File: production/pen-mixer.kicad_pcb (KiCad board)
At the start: 4 copper layers, 11 x 42 mm, 28 parts, among them J1 USB-C 16P, J2 BAT, U1 ISP1807-LR, U2 LSM6DS3TR-C, U3 MCP73831T-2ACI/OT, U4 TPS7A0533PDBV

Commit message: board fully routed verified
Claude-Session: https://claude.ai/code/session_01RCYT2QSY7BVZDeTyE9KrC4
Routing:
- net VBAT: track 39.4 -> 42.4 mm
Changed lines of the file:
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@@
+	)
+	(segment
+		(start 103.8 67.3)
+		(end 103.5 67.61)
+		(width 0.15)
+		(layer "F.Cu")
+		(net "VBAT")
 	)
 	(segment
@@
 	)
 	(segment
+		(start 103.5 64.89)
+		(end 103.8 65.2)
+		(width 0.15)
+		(layer "F.Cu")
+		(net "VBAT")
+	)
+	(segment
 		(start 103.501 64.8928)
 		(end 101.974 63.3652)
 		(width 0.15)
 		(layer "F.Cu")
+		(net "VBAT")
+	)
+	(segment
+		(start 103.8 65.2)
+		(end 103.8 67.3)
+		(width 0.15)
+		(layer "F.Cu")

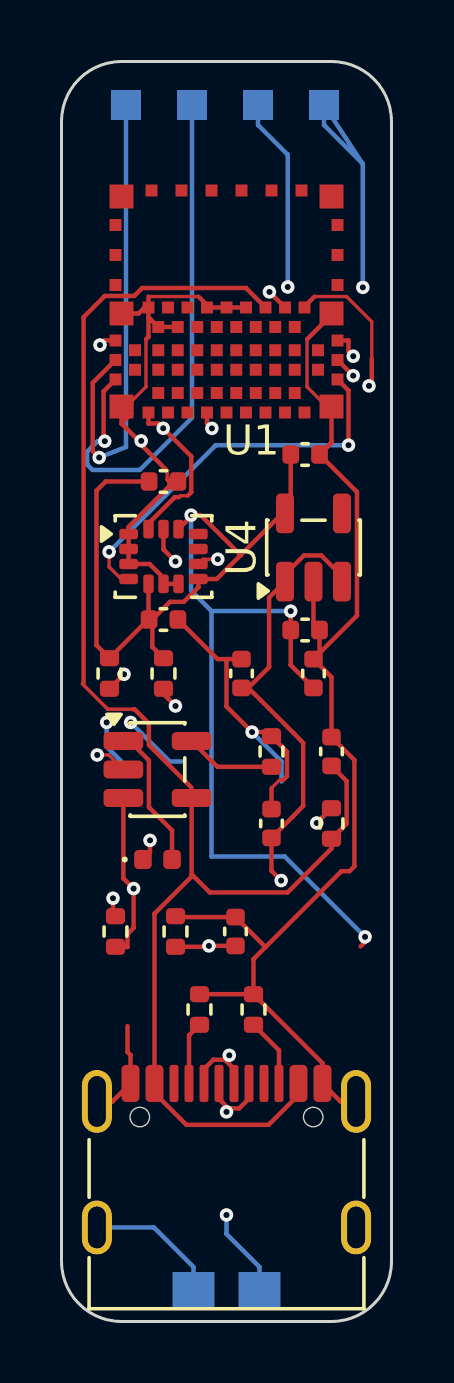
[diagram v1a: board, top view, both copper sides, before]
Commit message: unroute board
Claude-Session: https://claude.ai/code/session_01RCYT2QSY7BVZDeTyE9KrC4
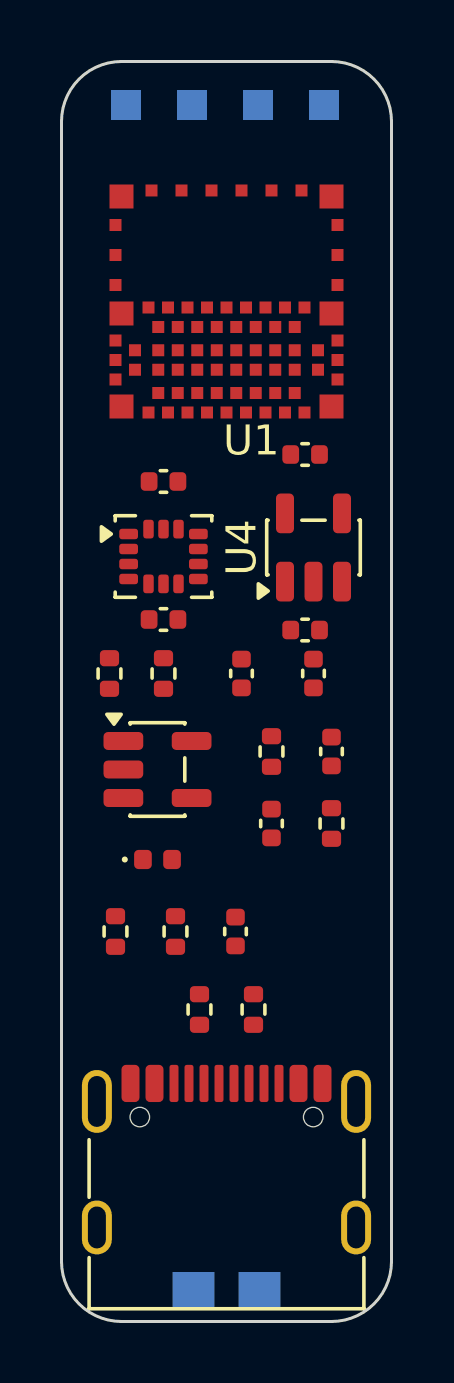
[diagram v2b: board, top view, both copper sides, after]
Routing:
- net GND: track 142.5 -> 0.00 mm, vias 4 -> 0
- net +3V3: track 77.3 -> 0.00 mm, vias 5 -> 0
- net VBUS: track 49.5 -> 0.00 mm
- net VBAT: track 42.4 -> 0.00 mm, vias 3 -> 0
- net USB_DP: track 33.5 -> 0.00 mm, vias 2 -> 0
- net SWDCLK: track 30.5 -> 0.00 mm, vias 2 -> 0
- net USB_DM: track 29.2 -> 0.00 mm, vias 2 -> 0
- net SWDIO: track 26.8 -> 0.00 mm, vias 2 -> 0
- net VBAT_SENSE: track 24.1 -> 0.00 mm, vias 3 -> 0
- net SCL: track 17.1 -> 0.00 mm, vias 3 -> 0
- net SDA: track 14.9 -> 0.00 mm, vias 2 -> 0
- net IMU_INT1: track 13.1 -> 0.00 mm, vias 2 -> 0
- net IMU_INT2: track 9.44 -> 0.00 mm, vias 2 -> 0
- net LED_A: track 7.23 -> 0.00 mm, vias 2 -> 0
- net CHG_STAT: track 4.74 -> 0.00 mm
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
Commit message: clean full reroute zero violations
Claude-Session: https://claude.ai/code/session_01RCYT2QSY7BVZDeTyE9KrC4
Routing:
- net GND: track 0.00 -> 98.3 mm, vias 0 -> 1
- net +3V3: track 0.00 -> 52.7 mm, vias 0 -> 2
- net VBUS: track 0.00 -> 45.5 mm, vias 0 -> 3
- net VBAT: track 0.00 -> 41.4 mm, vias 0 -> 6
- net USB_DP: track 0.00 -> 31.7 mm, vias 0 -> 2
- net USB_DM: track 0.00 -> 29.8 mm, vias 0 -> 2
- net VBAT_SENSE: track 0.00 -> 22.3 mm, vias 0 -> 2
- net SCL: track 0.00 -> 19.3 mm, vias 0 -> 3
- net SDA: track 0.00 -> 14.9 mm, vias 0 -> 2
- net IMU_INT1: track 0.00 -> 12.7 mm, vias 0 -> 2
- net SWDCLK: track 0.00 -> 11.8 mm, vias 0 -> 1
- net SWDIO: track 0.00 -> 10.5 mm, vias 0 -> 2
- net LED_A: track 0.00 -> 10.1 mm, vias 0 -> 2
- net IMU_INT2: track 0.00 -> 10.0 mm, vias 0 -> 2
- net CHG_STAT: track 0.00 -> 5.07 mm
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
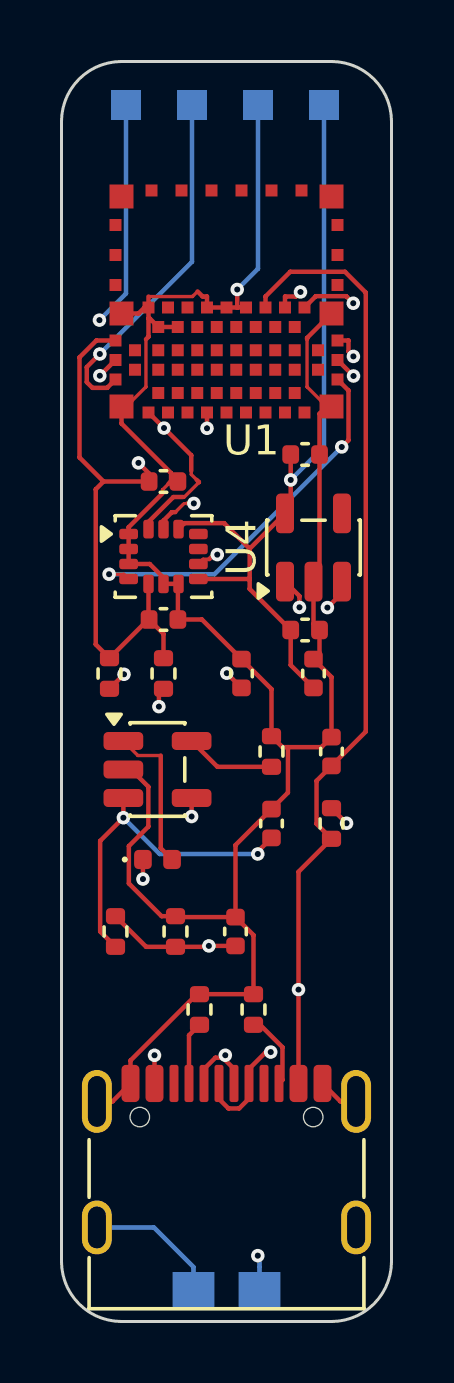
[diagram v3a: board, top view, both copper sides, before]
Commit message: fix wire tee gaps
Claude-Session: https://claude.ai/code/session_01RCYT2QSY7BVZDeTyE9KrC4
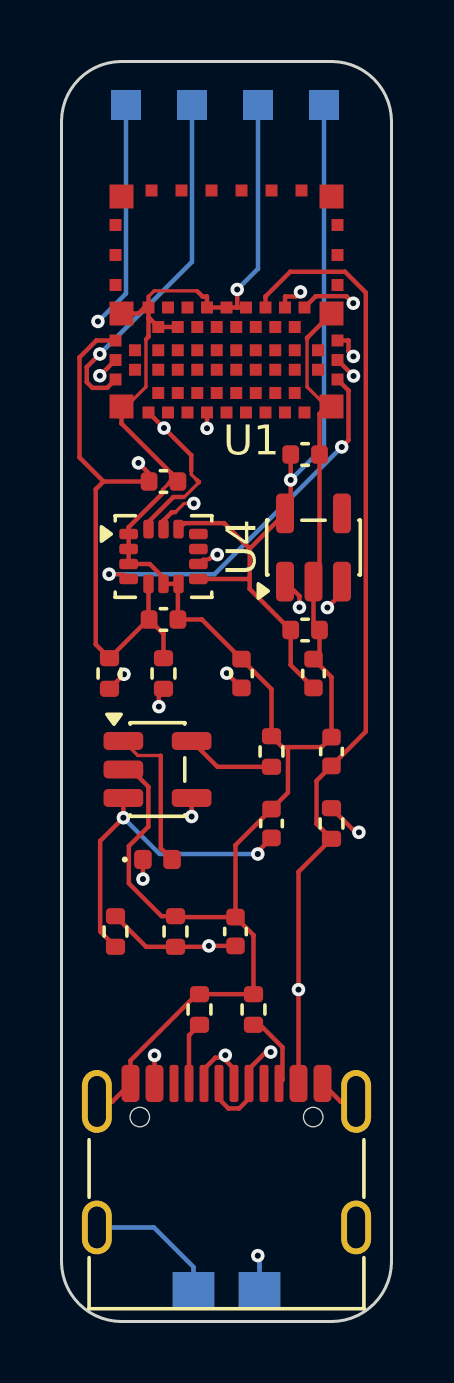
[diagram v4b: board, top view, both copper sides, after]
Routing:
- net LED_A: track 10.1 -> 11.1 mm
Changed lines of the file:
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@@
-	)
-	(segment
-		(start 100.1104 50.32)
-		(end 100.2804 50.15)
-		(width 0.1124)
-		(layer "F.Cu")
-		(net "GND")
 	)
 	(segment
@@
 	)
 	(segment
+		(start 100.2604 50.13)
+		(end 100.2804 50.15)
+		(width 0.1124)
+		(layer "F.Cu")
+		(net "GND")
+	)
+	(segment
 		(start 101.5452 71.0052)
 		(end 99.5752 71.0052)
@@
 		(end 101.8952 50.6852)
 		(width 0.15)
+		(layer "F.Cu")
+		(net "GND")
+	)
+	(segment
+		(start 98.6452 50.32)
+		(end 98.8352 50.13)
+		(width 0.1124)
 		(layer "F.Cu")
 		(net "GND")
@@
 	)
 	(segment
-		(start 98.6452 50.32)
-		(end 100.1104 50.32)
-		(width 0.1124)
-		(layer "F.Cu")
-		(net "GND")
-	)
-	(segment
 		(start 104.5852 53.9852)
 		(end 104.42 53.82)
 		(width 0.15)
+		(layer "F.Cu")
+		(net "GND")
+	)
+	(segment
+		(start 98.8352 50.13)
+		(end 100.2604 50.13)
+		(width 0.1124)
 		(layer "F.Cu")
 		(net "GND")
@@
 	)
 	(segment
-		(start 105.2465 67.8765)
+		(start 105.66 68.18)
+		(end 105.55 68.18)
+		(width 0.15)
+		(layer "F.Cu")
+		(net "LED_A")
+	)
+	(segment
+		(start 105.55 68.18)
 		(end 104.7452 67.3752)
 		(width 0.15)
@@
 	)
 	(via
-		(at 105.2465 67.8765)
+		(at 105.66 68.18)
 		(size 0.45)
 		(drill 0.2)
@@
 		(drill 0.2)
 		(layers "F.Cu" "B.Cu")
+		(net "LED_A")
+	)
+	(segment
+		(start 104.6002 67.2302)
+		(end 99.9468 67.2302)
+		(width 0.15)
+		(layer "In1.Cu")
+		(net "LED_A")
+	)
+	(segment
+		(start 98.4602 68.7168)
+		(end 98.4602 69.7378)
+		(width 0.15)
+		(layer "In1.Cu")
+		(net "LED_A")
+	)
+	(segment
+		(start 105.66 68.18)
+		(end 105.55 68.18)
+		(width 0.15)
+		(layer "In1.Cu")
+		(net "LED_A")
+	)
+	(segment
+		(start 105.55 68.18)
+		(end 104.6002 67.2302)
+		(width 0.15)
+		(layer "In1.Cu")
 		(net "LED_A")
 	)
@@
 		(start 99.9468 67.2302)
 		(end 98.4602 68.7168)
-		(width 0.15)
-		(layer "In1.Cu")
-		(net "LED_A")
-	)
-	(segment
-		(start 105.2465 67.8765)
-		(end 104.6002 67.2302)
-		(width 0.15)
-		(layer "In1.Cu")
-		(net "LED_A")
-	)
-	(segment
-		(start 98.4602 68.7168)
-		(end 98.4602 69.7378)
-		(width 0.15)
-		(layer "In1.Cu")
-		(net "LED_A")
-	)
-	(segment
-		(start 104.6002 67.2302)
-		(end 99.9468 67.2302)
 		(width 0.15)
 		(layer "In1.Cu")
@@
 	)
 	(via
-		(at 97.0099 51.1059)
-		(size 0.45)
-		(drill 0.2)
-		(layers "F.Cu" "B.Cu")
+		(at 96.96 51.15)
+		(size 0.45)
+		(drill 0.2)
+		(layers "F.Cu" "B.Cu")
+		(net "SWDIO")
+	)
+	(segment
+		(start 96.96 51.15)
+		(end 96.9658 51.15)
+		(width 0.15)
+		(layer "B.Cu")
 		(net "SWDIO")
 	)
@@
 	)
 	(segment
-		(start 97.0099 51.1059)
+		(start 96.9658 51.15)
 		(end 97.8952 50.2206)
 		(width 0.15)
@@
 	)
 	(segment
+		(start 96.96 51.15)
+		(end 96.96 51.1558)
+		(width 0.15)
+		(layer "In1.Cu")
+		(net "SWDIO")
+	)
+	(segment
+		(start 96.6077 52.5443)
+		(end 97.0219 52.9585)
+		(width 0.15)
+		(layer "In1.Cu")
+		(net "SWDIO")
+	)
+	(segment
+		(start 96.96 51.1558)
+		(end 96.6077 51.5081)
+		(width 0.15)
+		(layer "In1.Cu")
+		(net "SWDIO")
+	)
+	(segment
 		(start 96.6077 51.5081)
 		(end 96.6077 52.5443)
 		(width 0.15)
 		(layer "In1.Cu")
-		(net "SWDIO")
-	)
-	(segment
-		(start 96.6077 52.5443)
-		(end 97.0219 52.9585)
-		(width 0.15)
-		(layer "In1.Cu")
-		(net "SWDIO")
-	)
-	(segment
-		(start 97.0099 51.1059)
-		(end 96.6077 51.5081)
-		(width 0.15)
-		(layer "In1.Cu")

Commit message: silkscreen designators
Claude-Session: https://claude.ai/code/session_01RCYT2QSY7BVZDeTyE9KrC4
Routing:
- net VBUS: track 45.5 -> 46.1 mm
- net VBAT: track 41.4 -> 42.0 mm
